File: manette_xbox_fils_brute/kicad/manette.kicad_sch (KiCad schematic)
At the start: 31 parts, among them J1 THB001P, J2 THB001P, J3 Conn_01x20, X1 SW_Push, Y1 SW_Push

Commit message: redimensionnement de la carte
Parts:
- removed C1, C4: 100p, Capacitor_THT:CP_Radial_D5.0mm_P2.50mm, symbol Device:C
- removed C2, C5: 100n, Capacitor_THT:CP_Radial_D5.0mm_P2.50mm, symbol Device:C
- removed C3, C6: 10m, Capacitor_THT:CP_Radial_D5.0mm_P2.50mm, symbol Device:C
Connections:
- net A: now also J3.18 (Pin_18); no longer J3.17 (Pin_17)
- net X: now also J3.17 (Pin_17); no longer J3.18 (Pin_18)
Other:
- moved on the sheet: J3, MENU1, OPTION1, R_MENU1, R_OPTION1

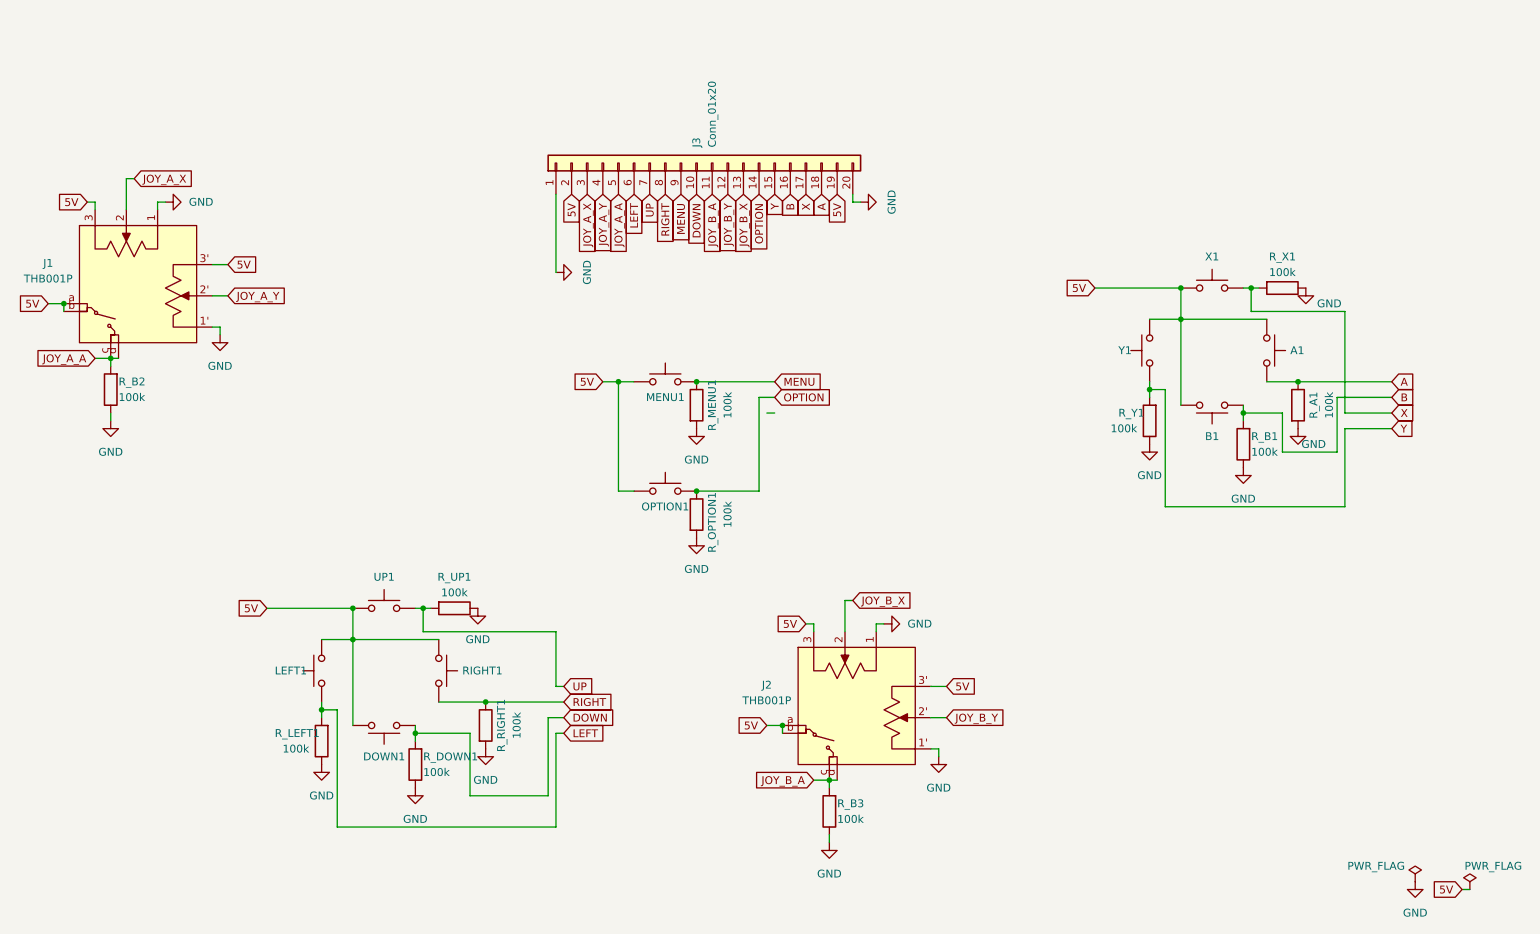
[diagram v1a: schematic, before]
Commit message: correction erreur & changement forme et trous pcb
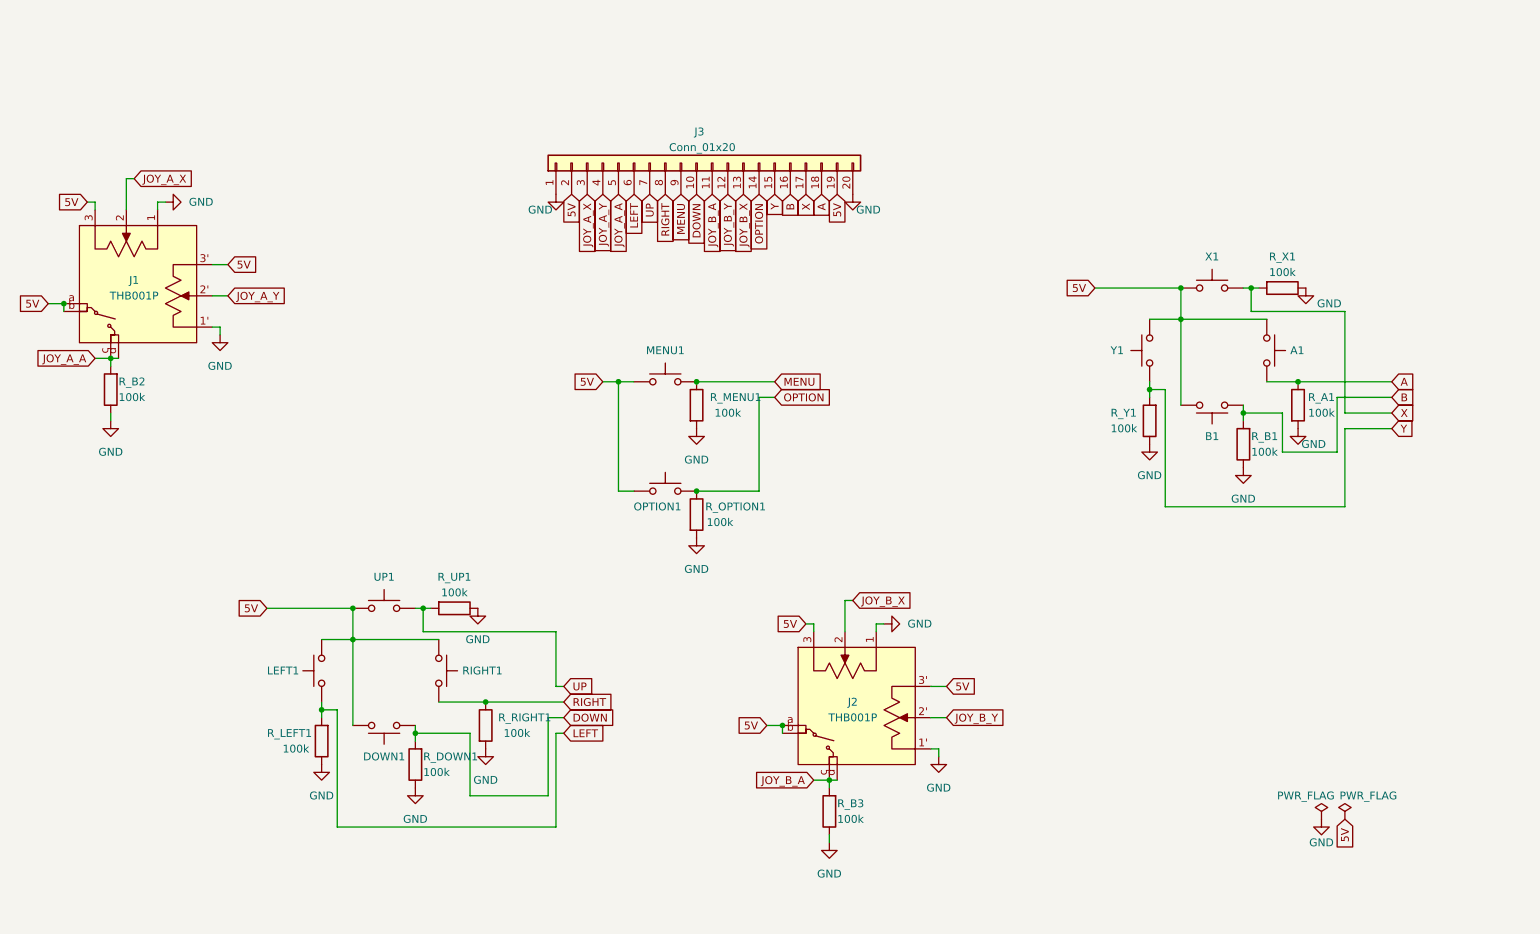
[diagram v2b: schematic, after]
